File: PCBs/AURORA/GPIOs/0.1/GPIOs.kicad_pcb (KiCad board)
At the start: 2 copper layers, 65 x 55 mm, 25 parts, among them J1 Conn_01x02_Pin, J10 Conn_01x02_Pin, J11 Conn_01x02_Pin, J12 Conn_01x02_Pin, J13 Conn_01x02_Pin, J14 Conn_01x02_Pin, J15 Conn_01x02_Pin, J16 Conn_01x02_Pin, J17 Conn_01x05_Pin, J2 Conn_01x02_Pin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

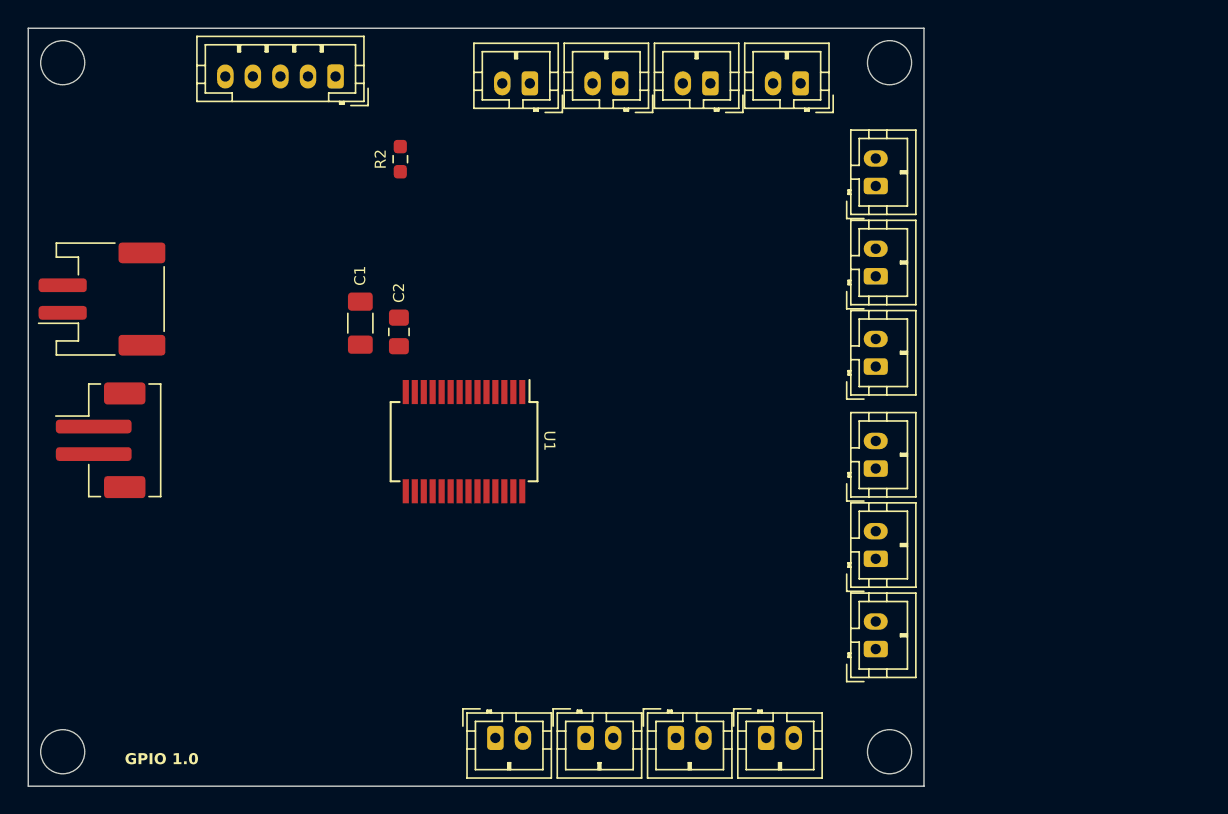
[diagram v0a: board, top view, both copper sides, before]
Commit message: Fixing audio issues, leave TRUNC off and at 24 bits
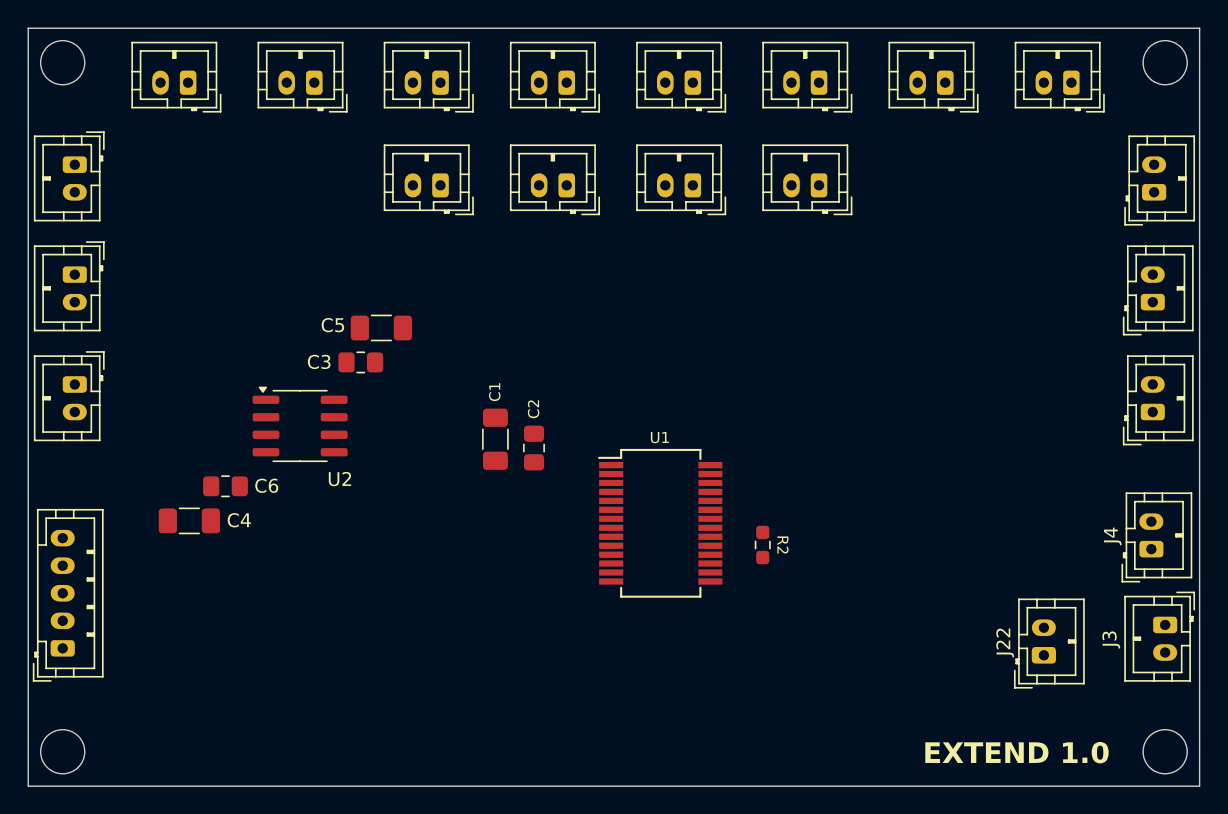
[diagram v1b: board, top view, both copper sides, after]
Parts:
- added C3: 0.1U, Capacitor_SMD:C_0805_2012Metric_Pad1.18x1.45mm_HandSolder, F.Cu at (110.0, 87.8)
- added C4: 10U, Capacitor_SMD:C_1206_3216Metric_Pad1.33x1.80mm_HandSolder, F.Cu at (97.6, 99.2)
- added C5: 10U, Capacitor_SMD:C_1206_3216Metric_Pad1.33x1.80mm_HandSolder, F.Cu at (111.5, 85.2)
- added C6: 0.1U, Capacitor_SMD:C_0805_2012Metric_Pad1.18x1.45mm_HandSolder, F.Cu at (100.2, 96.7)
- added J18: Conn_01x02_Male, Connector_JST:JST_PH_B2B-PH-K_1x02_P2.00mm_Vertical, F.Cu at (97.5, 67.5)
- added J19: Conn_01x02_Male, Connector_JST:JST_PH_B2B-PH-K_1x02_P2.00mm_Vertical, F.Cu at (89.3, 73.4)
- added J20: Conn_01x02_Male, Connector_JST:JST_PH_B2B-PH-K_1x02_P2.00mm_Vertical, F.Cu at (167.6, 75.4)
- added J21: Conn_01x02_Male, Connector_JST:JST_PH_B2B-PH-K_1x02_P2.00mm_Vertical, F.Cu at (161.6, 67.5)
- added J22: Conn_01x02_Male, Connector_JST:JST_PH_B2B-PH-K_1x02_P2.00mm_Vertical, F.Cu at (159.6, 109.0)
- added U2: TCA9517DR, Package_SO:SOIC-8_3.9x4.9mm_P1.27mm, F.Cu at (105.6, 92.4)
- J3: footprint Connector_JST:JST_PH_S2B-PH-SM4-TB_1x02-1MP_P2.00mm_Horizontal -> Connector_JST:JST_PH_B2B-PH-K_1x02_P2.00mm_Vertical
- J4: footprint Connector_JST:JST_PH_B2B-PH-SM4-TB_1x02-1MP_P2.00mm_Vertical -> Connector_JST:JST_PH_B2B-PH-K_1x02_P2.00mm_Vertical
- moved J3 80.7 mm to (168.4, 106.8), turned to -90 degrees
- moved J4 76.7 mm to (167.4, 101.3), turned to 90 degrees
- moved J16 53.2 mm to (167.5, 91.3), turned to 90 degrees
- moved J15 51.9 mm to (167.5, 83.4), turned to 90 degrees
- moved J17 46.0 mm to (88.4, 108.5), turned to 90 degrees
- moved J2 41.9 mm to (89.3, 81.4), turned to -90 degrees
- moved J7 41.4 mm to (106.7, 67.5), turned to 180 degrees
- moved J14 41.4 mm to (143.3, 74.9), turned to 180 degrees
- moved J12 41.4 mm to (152.4, 67.5), turned to 180 degrees
- moved J13 40.5 mm to (134.1, 74.9), turned to 180 degrees
- moved J1 39.6 mm to (89.3, 89.3), turned to -90 degrees
- moved R2 38.4 mm to (139.2, 101.0), turned to -90 degrees
- moved J11 34.8 mm to (143.3, 67.5), turned to 180 degrees
- moved J8 34.6 mm to (115.8, 67.5), turned to 180 degrees
- moved J10 31.0 mm to (134.1, 67.5), turned to 180 degrees
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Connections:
- net GPA0 renamed SPDIF_RESET
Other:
- board size 65 x 55 mm -> 85 x 55 mm
- board text added: "EXTEND 1.0"
- board text added: "SDF_RST"
- board text removed: "GPIO 1.0"
